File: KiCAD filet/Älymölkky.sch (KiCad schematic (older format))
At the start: 39 parts, among them P0.18_TP1 Conn_01x01_Male, U1 nRF52810-QCxx, X1 32MHz Crystal, X2 32.768 kHz Crystal

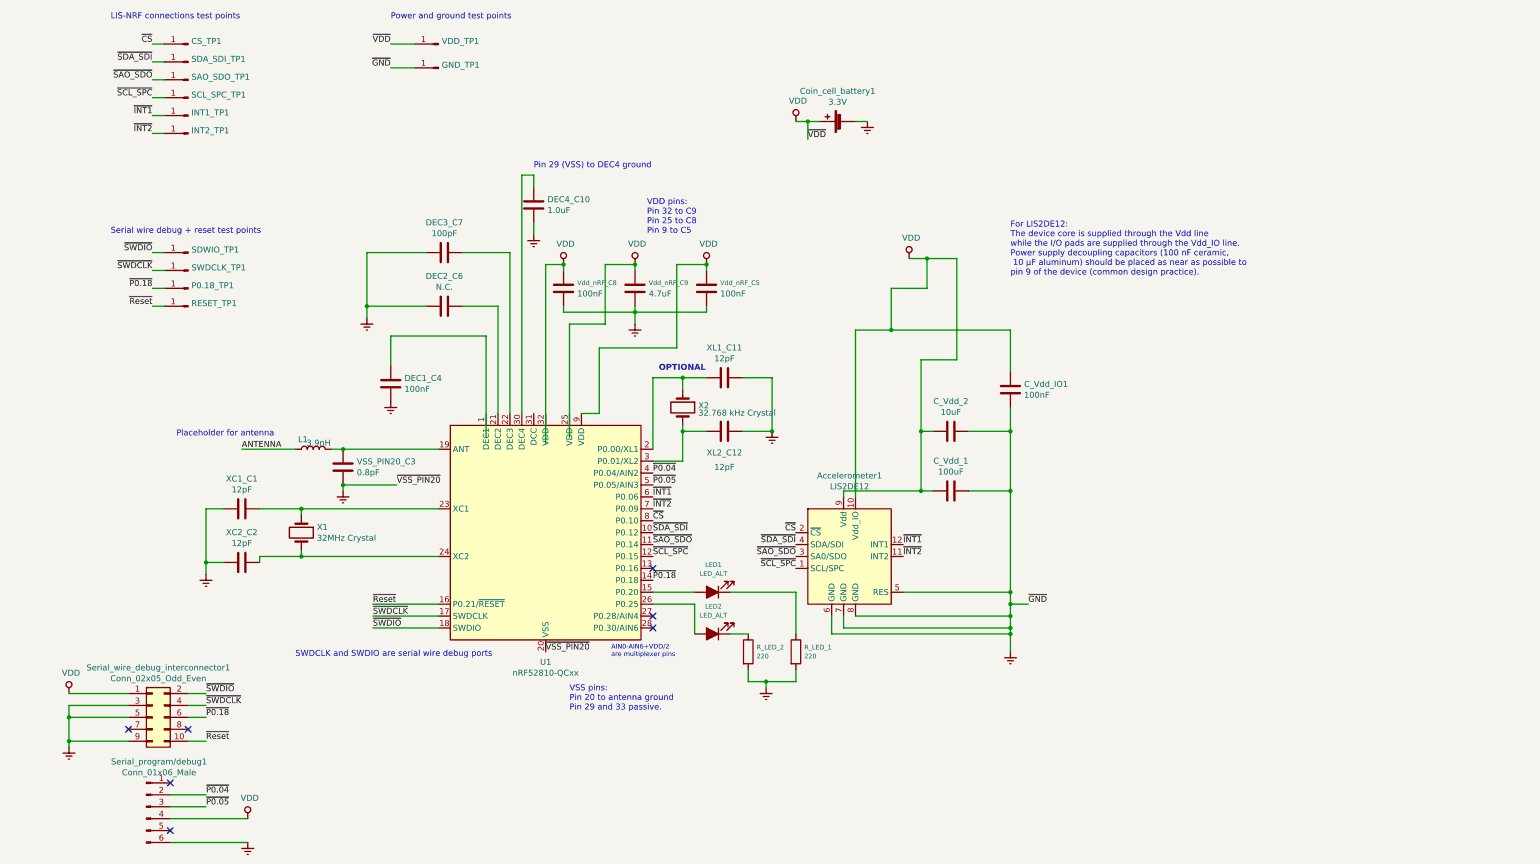
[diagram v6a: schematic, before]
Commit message: Changed the circuit to allow internal DC/DC converter to be used
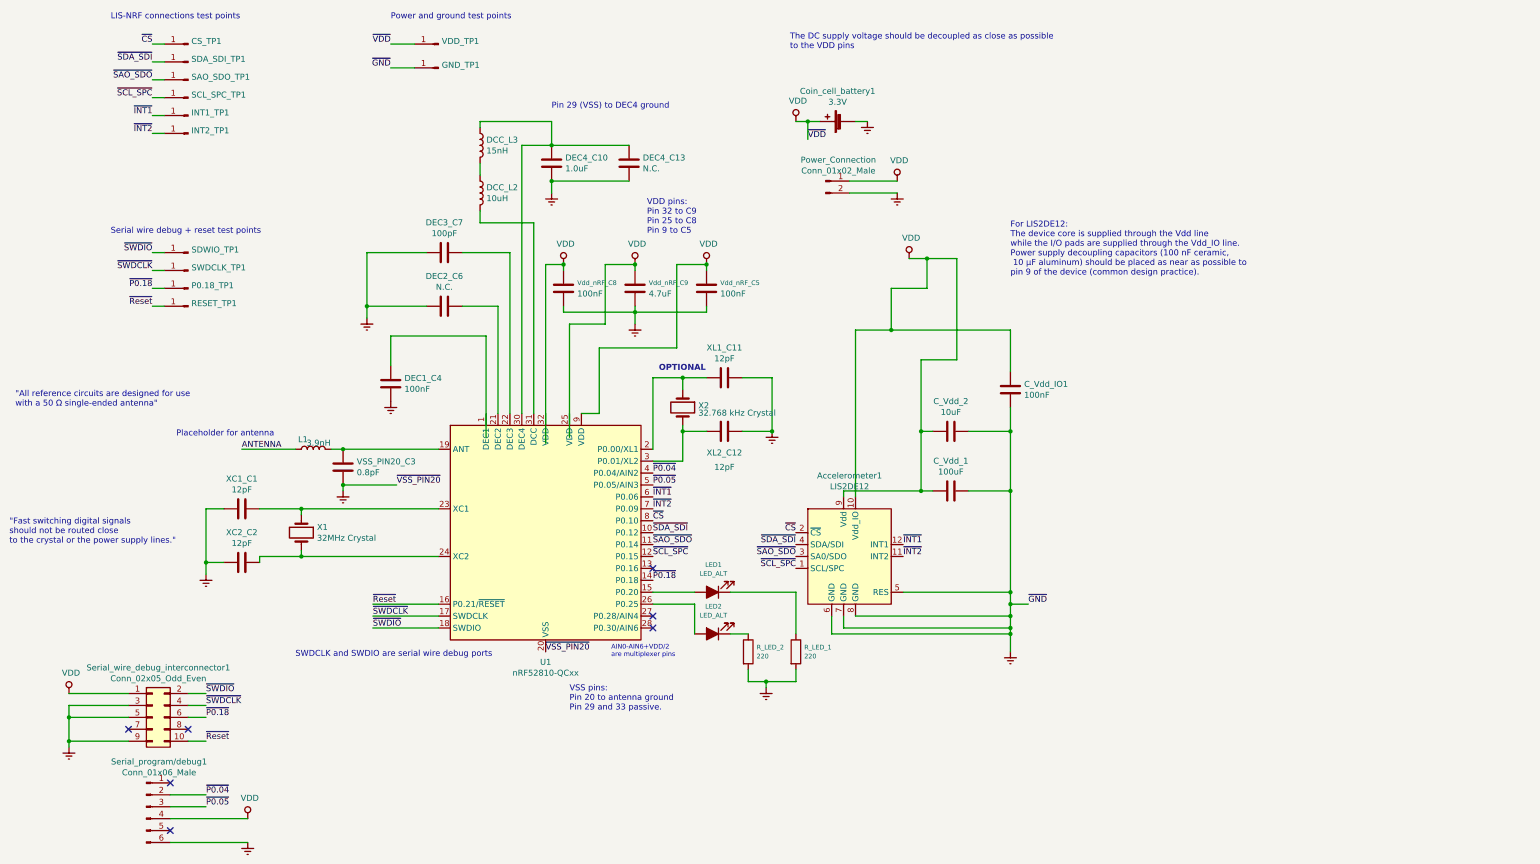
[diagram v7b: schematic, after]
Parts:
- added DCC_L2: 10uH, symbol Device:L
- added DCC_L3: 15nH, symbol Device:L
- added DEC4_C13: N.C., Capacitor_SMD:C_0805_2012Metric_Pad1.15x1.40mm_HandSolder, symbol Device:C
- added Power_Connection: Conn_01x02_Male, symbol Connector:Conn_01x02_Male
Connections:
- net Earth: now also DEC4_C13.2, Power_Connection.2 (Pin_2)
- net VDD: now also Power_Connection.1 (Pin_1)
- net at DEC4_C10.1, U1.30 (DEC4): now also DCC_L3.1, DEC4_C13.1
- net at U1.31 (DCC): now also DCC_L2.2
- new net: DCC_L2.1, DCC_L3.2
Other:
- note added: ""All reference circuits are designed for use\nwith a 50 Ω single-ended antenna""
- note added: ""Fast switching digital signals\nshould not be routed close\nto the crystal or the power supply lines.""
- note added: "The DC supply voltage should be decoupled as close as possible\nto the VDD pins"
- moved on the sheet: DEC4_C10
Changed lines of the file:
@@
 encoding utf-8
 Sheet 1 1
-Title ""
+Title "ÄlyMölkky with internal DC/DC regulator setup"
 Date ""
 Rev ""
@@
 L Device:C DEC4_C10
 U 1 1 5C61DF93
-P 4950 2300
-F 0 "DEC4_C10" H 5065 2346 50  0000 L CNN
-F 1 "1.0uF" H 5065 2255 50  0000 L CNN
-F 2 "Capacitor_SMD:C_0805_2012Metric_Pad1.15x1.40mm_HandSolder" H 4988 2150 50  0001 C CNN
-F 3 "~" H 4950 2300 50  0001 C CNN
-	1    4950 2300
-	1    0    0    -1
-$EndComp
-Text Notes 4950 2000 0    50   ~ 0
+P 5100 1950
+F 0 "DEC4_C10" H 5215 1996 50  0000 L CNN
+F 1 "1.0uF" H 5215 1905 50  0000 L CNN
+F 2 "Capacitor_SMD:C_0805_2012Metric_Pad1.15x1.40mm_HandSolder" H 5138 1800 50  0001 C CNN
+F 3 "~" H 5100 1950 50  0001 C CNN
+	1    5100 1950
+	1    0    0    -1
+$EndComp
+Text Notes 5100 1500 0    50   ~ 0
 Pin 29 (VSS) to DEC4 ground
 $Comp
@@
 	2200 5300 2200 5400
 Connection ~ 2200 5300
-Wire Wire Line
-	4850 4050 4850 2050
-Wire Wire Line
-	4850 2050 4950 2050
-Wire Wire Line
-	4950 2050 4950 2150
 $Comp
 L power:Earth #PWR0107
 U 1 1 5C629483
-P 4950 2550
-F 0 "#PWR0107" H 4950 2300 50  0001 C CNN
-F 1 "Earth" H 4950 2400 50  0001 C CNN
-F 2 "" H 4950 2550 50  0001 C CNN
-F 3 "~" H 4950 2550 50  0001 C CNN
-	1    4950 2550
-	1    0    0    -1
-$EndComp
-Wire Wire Line
-	4950 2450 4950 2550
+P 5100 2200
+F 0 "#PWR0107" H 5100 1950 50  0001 C CNN
+F 1 "Earth" H 5100 2050 50  0001 C CNN
+F 2 "" H 5100 2200 50  0001 C CNN
+F 3 "~" H 5100 2200 50  0001 C CNN
+	1    5100 2200
+	1    0    0    -1
+$EndComp
 $Comp
 L Device:C DEC3_C7
@@
 Wire Wire Line
 	1750 3150 1850 3150
+$Comp
+L Device:C DEC4_C13
+U 1 1 5C664DC4
+P 5750 1950
+F 0 "DEC4_C13" H 5865 1996 50  0000 L CNN
+F 1 "N.C." H 5865 1905 50  0000 L CNN
+F 2 "Capacitor_SMD:C_0805_2012Metric_Pad1.15x1.40mm_HandSolder" H 5788 1800 50  0001 C CNN
+F 3 "~" H 5750 1950 50  0001 C CNN
+	1    5750 1950
+	1    0    0    -1
+$EndComp
+Wire Wire Line
+	5100 2100 5100 2200
+Wire Wire Line
+	5750 2100 5100 2100
+Connection ~ 5100 2100
+Wire Wire Line
+	5100 1800 5750 1800
+Wire Wire Line
+	4850 4050 4850 1800
+Wire Wire Line
+	4850 1800 5100 1800
+Connection ~ 5100 1800
+$Comp
+L Device:L DCC_L2
+U 1 1 5C68445F
+P 4500 2200
+F 0 "DCC_L2" H 4553 2246 50  0000 L CNN
+F 1 "10uH" H 4553 2155 50  0000 L CNN
+F 2 "" H 4500 2200 50  0001 C CNN
+F 3 "~" H 4500 2200 50  0001 C CNN
+	1    4500 2200
+	1    0    0    -1
+$EndComp
+$Comp
+L Device:L DCC_L3
+U 1 1 5C6844D9
+P 4500 1800
+F 0 "DCC_L3" H 4553 1846 50  0000 L CNN
+F 1 "15nH" H 4553 1755 50  0000 L CNN
+F 2 "" H 4500 1800 50  0001 C CNN
+F 3 "~" H 4500 1800 50  0001 C CNN
+	1    4500 1800
+	1    0    0    -1
+$EndComp
+Wire Wire Line
+	4950 4050 4950 2450
+Wire Wire Line
+	4950 2450 4500 2450
+Wire Wire Line
+	4500 2450 4500 2350
+Wire Wire Line
+	4500 2050 4500 1950
+Wire Wire Line
+	4500 1650 4500 1600
+Wire Wire Line
+	4500 1600 5100 1600
+Wire Wire Line
+	5100 1600 5100 1800
+Text Notes 600  4000 0    50   ~ 0
+"All reference circuits are designed for use\nwith a 50 Ω single-ended antenna"
+Text Notes 7100 1000 0    50   ~ 0
+The DC supply voltage should be decoupled as close as possible\nto the VDD pins
+Text Notes 550  5150 0    50   ~ 0
+"Fast switching digital signals\nshould not be routed close\nto the crystal or the power supply lines."
+$Comp
+L Connector:Conn_01x02_Male Power_Connection
+U 1 1 5C6A2D8F
+P 7400 2100
+F 0 "Power_Connection" H 7506 2278 50  0000 C CNN
+F 1 "Conn_01x02_Male" H 7506 2187 50  0000 C CNN
+F 2 "" H 7400 2100 50  0001 C CNN
+F 3 "~" H 7400 2100 50  0001 C CNN
+	1    7400 2100
+	1    0    0    -1
+$EndComp
+$Comp
+L power:VDD #PWR?
+U 1 1 5C6A36D5
+P 8000 2100
+F 0 "#PWR?" H 8000 1950 50  0001 C CNN
+F 1 "VDD" H 8017 2273 50  0000 C CNN
+F 2 "" H 8000 2100 50  0001 C CNN
+F 3 "" H 8000 2100 50  0001 C CNN
+	1    8000 2100
+	1    0    0    -1
+$EndComp
+$Comp
+L power:Earth #PWR?
+U 1 1 5C6A3736
+P 8000 2200
+F 0 "#PWR?" H 8000 1950 50  0001 C CNN
+F 1 "Earth" H 8000 2050 50  0001 C CNN
+F 2 "" H 8000 2200 50  0001 C CNN
+F 3 "~" H 8000 2200 50  0001 C CNN
+	1    8000 2200
+	1    0    0    -1
+$EndComp
+Wire Wire Line
+	8000 2100 7600 2100
+Wire Wire Line
+	7600 2200 8000 2200
 $EndSCHEMATC

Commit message: Added pcb layouts for components and initialized the layout work
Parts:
- added hupivia1: Conn_01x01_Male, Connector_PinHeader_2.54mm:PinHeader_1x01_P2.54mm_Vertical, symbol Connector:Conn_01x01_Male
- DCC_L2, DCC_L3: footprint (none) -> Capacitor_SMD:C_0805_2012Metric_Pad1.15x1.40mm_HandSolder
- Power_Connection1: renamed from Power_Connection; value Conn_01x02_Male -> Conn_01x02_Female; footprint (none) -> Connector_PinHeader_2.54mm:PinHeader_1x02_P2.54mm_Vertical; symbol Connector:Conn_01x02_Male -> Connector:Conn_01x02_Female
- VSS_PIN20_C3, XC1_C1, XC2_C2, XL1_C11, XL2_C12: footprint (none) -> Capacitor_SMD:C_0402_1005Metric
- X1: footprint (none) -> Custom_footprints_alymolkky:Crystal_3.2x2.5x0.8; symbol Device:Crystal -> Device:Crystal_GND24
- X2: footprint (none) -> Crystal:Crystal_SMD_3215-2Pin_3.2x1.5mm
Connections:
- net Earth: now also Power_Connection1.1 (Pin_1), X1.2, X1.4, hupivia1.1 (Pin_1); no longer Power_Connection1.2 (Pin_2)
- net VDD: now also Power_Connection1.2 (Pin_2), U1.25 (VDD), U1.32 (VDD); no longer Power_Connection1.1 (Pin_1)
- net at DEC1_C4.1: now also U1.1 (DEC1)
- net at U1.24 (XC2), XC2_C2.1: now also X1.3; no longer X1.2
- no-connect marks 7 -> 8
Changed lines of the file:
@@
 U 1 1 5C5CAB8B
 P 3100 4350
-F 0 "L1" V 3153 4396 50  0000 L TNN
-F 1 "3.9nH" V 3153 4305 50  0000 C CNN
+F 0 "L1" V 3000 4350 50  0000 L TNN
+F 1 "3.9nH" V 3200 4350 50  0000 C CNN
 F 2 "Resistor_SMD:R_0805_2012Metric_Pad1.15x1.40mm_HandSolder" H 3100 4350 50  0001 C CNN
 F 3 "~" H 3100 4350 50  0001 C CNN
@@
 $EndComp
 Wire Wire Line
-	5050 2800 5200 2800
-Wire Wire Line
 	5200 2800 5200 2850
 Text Notes 5900 2550 0    50   ~ 0
@@
 Pin 29 (VSS) to DEC4 ground
 $Comp
-L Device:Crystal X1
+L Device:Crystal_GND24 X1
 U 1 1 5C620103
 P 3000 5050
-F 0 "X1" V 2954 5181 50  0000 L CNN
-F 1 "32MHz Crystal" V 3045 5181 50  0000 L CNN
-F 2 "" H 3000 5050 50  0001 C CNN
-F 3 "~" H 3000 5050 50  0001 C CNN
+F 0 "X1" V 2950 5300 50  0000 L CNN
+F 1 "32MHz Crystal" V 3050 5300 50  0000 L CNN
+F 2 "Custom_footprints_alymolkky:Crystal_3.2x2.5x0.8" H 3000 5050 50  0001 C CNN
+F 3 "https://www.mouser.fi/ProductDetail/ECS/ECS-320-8-33-RWY-TR?qs=sGAEpiMZZMsBj6bBr9Q9abMK2mGYOCsJNNEntTUpRFbSy%252b%2fVo4P4%252bg%3d%3d" H 3000 5050 50  0001 C CNN
 	1    3000 5050
 	0    1    1    0
@@
 F 0 "XC1_C1" V 2248 4850 50  0000 C CNN
 F 1 "12pF" V 2339 4850 50  0000 C CNN
-F 2 "" H 2538 4700 50  0001 C CNN
+F 2 "Capacitor_SMD:C_0402_1005Metric" H 2538 4700 50  0001 C CNN
 F 3 "~" H 2500 4850 50  0001 C CNN
 	1    2500 4850
@@
 F 0 "XC2_C2" V 2248 5300 50  0000 C CNN
 F 1 "12pF" V 2339 5300 50  0000 C CNN
-F 2 "" H 2538 5150 50  0001 C CNN
+F 2 "Capacitor_SMD:C_0402_1005Metric" H 2538 5150 50  0001 C CNN
 F 3 "~" H 2500 5300 50  0001 C CNN
 	1    2500 5300
@@
 	3550 3150 3550 3250
 Connection ~ 3550 3150
-Wire Wire Line
-	2950 4350 2500 4350
 $Comp
 L Device:Crystal X2
@@
 F 0 "X2" V 6154 4131 50  0000 L TNN
 F 1 "32.768 kHz Crystal" V 6245 4131 50  0000 L CNN
-F 2 "" H 6200 4000 50  0001 C CNN
-F 3 "~" H 6200 4000 50  0001 C CNN
+F 2 "Crystal:Crystal_SMD_3215-2Pin_3.2x1.5mm" H 6200 4000 50  0001 C CNN
+F 3 "https://www.mouser.fi/ProductDetail/Epson-Timing/FC-135-327680KA-AC3?qs=sGAEpiMZZMsBj6bBr9Q9aZLqXgWtLYAXwYm2VNVNmc4%3D" H 6200 4000 50  0001 C CNN
 	1    6200 4000
 	0    1    1    0
@@
 F 0 "XL1_C11" V 6298 3750 50  0000 C CNN
 F 1 "12pF" V 6389 3750 50  0000 C CNN
-F 2 "" H 6588 3600 50  0001 C CNN
+F 2 "Capacitor_SMD:C_0402_1005Metric" H 6588 3600 50  0001 C CNN
 F 3 "~" H 6550 3750 50  0001 C CNN
 	1    6550 3750
@@
 F 0 "XL2_C12" V 6700 4200 50  0000 C TNN
 F 1 "12pF" V 6850 4200 50  0000 C CNN
-F 2 "" H 6588 4050 50  0001 C CNN
+F 2 "Capacitor_SMD:C_0402_1005Metric" H 6588 4050 50  0001 C CNN
 F 3 "~" H 6550 4200 50  0001 C CNN
 	1    6550 4200
@@
 F 0 "VSS_PIN20_C3" H 3465 4546 50  0000 L CNN
 F 1 "0.8pF" H 3465 4455 50  0000 L CNN
-F 2 "" H 3388 4350 50  0001 C CNN
+F 2 "Capacitor_SMD:C_0402_1005Metric" H 3388 4350 50  0001 C CNN
 F 3 "~" H 3350 4500 50  0001 C CNN
 	1    3350 4500
@@
 Wire Wire Line
 	5350 4050 5500 4050
-Wire Wire Line
-	5250 3300 5250 4250
-Wire Wire Line
-	5050 2800 5050 4300
-Wire Wire Line
-	4550 3400 4550 4250
 $Comp
 L Device:Battery_Cell Coin_cell_battery1
@@
 F 0 "DCC_L2" H 4553 2246 50  0000 L CNN
 F 1 "10uH" H 4553 2155 50  0000 L CNN
-F 2 "" H 4500 2200 50  0001 C CNN
+F 2 "Capacitor_SMD:C_0805_2012Metric_Pad1.15x1.40mm_HandSolder" H 4500 2200 50  0001 C CNN
 F 3 "~" H 4500 2200 50  0001 C CNN
 	1    4500 2200
@@
 F 0 "DCC_L3" H 4553 1846 50  0000 L CNN
 F 1 "15nH" H 4553 1755 50  0000 L CNN
-F 2 "" H 4500 1800 50  0001 C CNN
+F 2 "Capacitor_SMD:C_0805_2012Metric_Pad1.15x1.40mm_HandSolder" H 4500 1800 50  0001 C CNN
 F 3 "~" H 4500 1800 50  0001 C CNN
 	1    4500 1800
@@
 "Fast switching digital signals\nshould not be routed close\nto the crystal or the power supply lines."
 $Comp
-L Connector:Conn_01x02_Male Power_Connection
+L Connector:Conn_01x02_Female Power_Connection1
 U 1 1 5C6A2D8F
-P 7400 2100
-F 0 "Power_Connection" H 7506 2278 50  0000 C CNN
-F 1 "Conn_01x02_Male" H 7506 2187 50  0000 C CNN
-F 2 "" H 7400 2100 50  0001 C CNN
-F 3 "~" H 7400 2100 50  0001 C CNN
-	1    7400 2100
-	1    0    0    -1
-$EndComp
-$Comp
-L power:VDD #PWR?
+P 7400 2200
+F 0 "Power_Connection1" H 7294 1875 50  0000 C CNN
+F 1 "Conn_01x02_Female" H 7294 1966 50  0000 C CNN
+F 2 "Connector_PinHeader_2.54mm:PinHeader_1x02_P2.54mm_Vertical" H 7400 2200 50  0001 C CNN
+F 3 "~" H 7400 2200 50  0001 C CNN
+	1    7400 2200
+	-1   0    0    1
+$EndComp
+$Comp
+L power:VDD #PWR0120
 U 1 1 5C6A36D5
 P 8000 2100
-F 0 "#PWR?" H 8000 1950 50  0001 C CNN
+F 0 "#PWR0120" H 8000 1950 50  0001 C CNN
 F 1 "VDD" H 8017 2273 50  0000 C CNN
 F 2 "" H 8000 2100 50  0001 C CNN
@@
 $EndComp
 $Comp
-L power:Earth #PWR?
+L power:Earth #PWR0121
 U 1 1 5C6A3736
 P 8000 2200
-F 0 "#PWR?" H 8000 1950 50  0001 C CNN
+F 0 "#PWR0121" H 8000 1950 50  0001 C CNN
 F 1 "Earth" H 8000 2050 50  0001 C CNN
 F 2 "" H 8000 2200 50  0001 C CNN
@@
 Wire Wire Line
 	7600 2200 8000 2200
+$Comp
+L power:Earth #PWR0122
+U 1 1 5C6B5FA7
+P 3200 5050
+F 0 "#PWR0122" H 3200 4800 50  0001 C CNN
+F 1 "Earth" H 3200 4900 50  0001 C CNN
+F 2 "" H 3200 5050 50  0001 C CNN
+F 3 "~" H 3200 5050 50  0001 C CNN
+	1    3200 5050
+	1    0    0    -1
+$EndComp
+$Comp
+L power:Earth #PWR0123
+U 1 1 5C6B600F
+P 2800 5050
+F 0 "#PWR0123" H 2800 4800 50  0001 C CNN
+F 1 "Earth" H 2800 4900 50  0001 C CNN
+F 2 "" H 2800 5050 50  0001 C CNN
+F 3 "~" H 2800 5050 50  0001 C CNN
+	1    2800 5050
+	1    0    0    -1
+$EndComp
+Wire Wire Line
+	5050 4050 5050 2800
+Wire Wire Line
+	5050 2800 5200 2800
+Wire Wire Line
+	5250 4050 5250 3300
+Wire Wire Line
+	4550 4050 4550 3400
+$Comp
+L power:PWR_FLAG #FLG0101
+U 1 1 5C67417B
+P 2800 7450
+F 0 "#FLG0101" H 2800 7525 50  0001 C CNN
+F 1 "PWR_FLAG" H 2800 7624 50  0000 C CNN
+F 2 "" H 2800 7450 50  0001 C CNN
+F 3 "~" H 2800 7450 50  0001 C CNN
+	1    2800 7450
+	1    0    0    -1
+$EndComp
+$Comp
+L power:PWR_FLAG #FLG0102
+U 1 1 5C6741E3
+P 2800 7650
+F 0 "#FLG0102" H 2800 7725 50  0001 C CNN
+F 1 "PWR_FLAG" H 2800 7824 50  0000 C CNN
+F 2 "" H 2800 7650 50  0001 C CNN
+F 3 "~" H 2800 7650 50  0001 C CNN
+	1    2800 7650
+	1    0    0    -1
+$EndComp
+Wire Wire Line
+	2800 7650 2550 7650
+Connection ~ 2550 7650
+Wire Wire Line
+	2800 7450 2550 7450
+Connection ~ 2550 7450
+Wire Wire Line
+	2500 4350 2950 4350
+NoConn ~ 2500 4350
+$Comp
+L Connector:Conn_01x01_Male hupivia1
+U 1 1 5C69FFA8
+P 4150 1450
+F 0 "hupivia1" H 4122 1426 50  0000 R CNN
+F 1 "Conn_01x01_Male" H 4123 1471 50  0001 R CNN
+F 2 "Connector_PinHeader_2.54mm:PinHeader_1x01_P2.54mm_Vertical" H 4150 1450 50  0001 C CNN
+F 3 "~" H 4150 1450 50  0001 C CNN
+	1    4150 1450
+	-1   0    0    1
+$EndComp
+Text Label 3750 1450 2    50   ~ 0
+~GND
+Wire Wire Line
+	3750 1450 3950 1450
 $EndSCHEMATC
